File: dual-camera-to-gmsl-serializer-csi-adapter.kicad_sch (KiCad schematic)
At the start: 126 parts, among them J1 Conn_FFC_WE_68715014022, J2 Conn_FFC_WE_68715014022, J3 Conn_FFC_WE_68715014022, J4 JST_SH_1x4_SM04B-SRSS-TB-LF-SN, J5 JST_SH_1x4_SM04B-SRSS-TB-LF-SN, U1 TPS2117DRLR, U2 TPS2117DRLR, U3 AP62301_TSOT

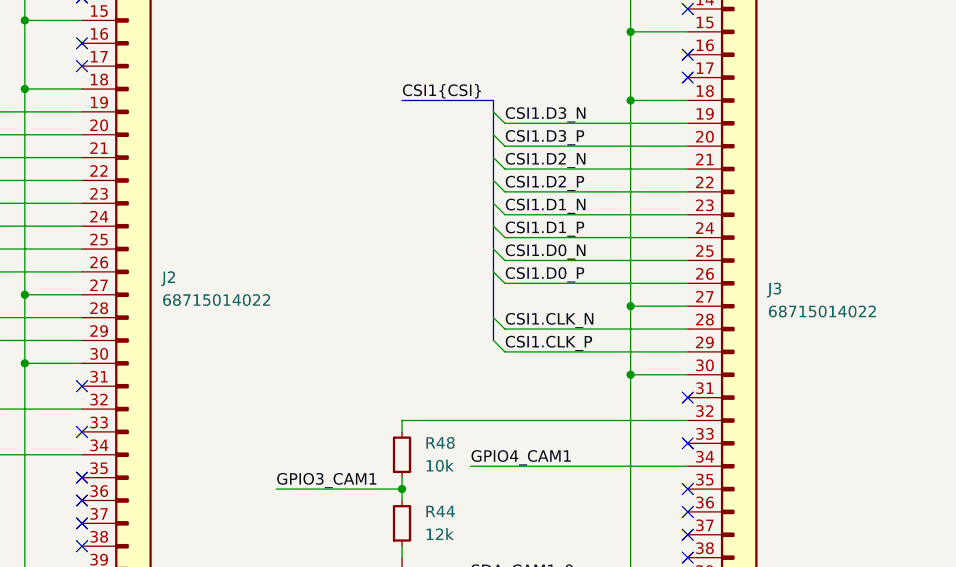
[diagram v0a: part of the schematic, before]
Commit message: [#70359] Schematic: Swap J2 with J3
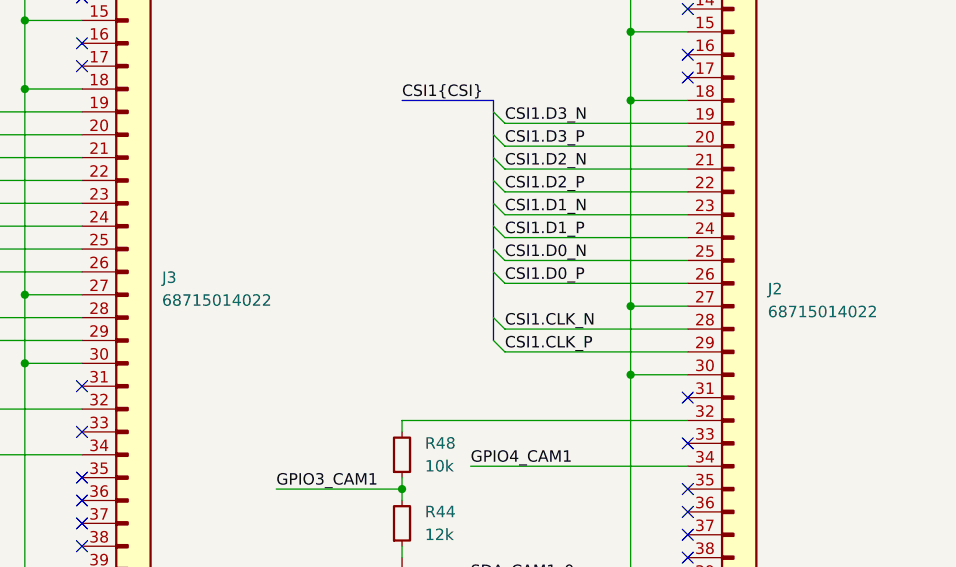
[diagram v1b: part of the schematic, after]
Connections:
- net 3V3_0: now also J3.47, J3.48; no longer J2.47, J2.48
- net 3V3_1: now also J2.47, J2.48; no longer J3.47, J3.48
- net 5V_0: now also J3.49, J3.50; no longer J2.49, J2.50
- net 5V_1: now also J2.49, J2.50; no longer J3.49, J3.50
- net CSI0.CLK_N: now also J3.28; no longer J2.28
- net CSI0.CLK_P: now also J3.29; no longer J2.29
- net CSI0.D0_N: now also J3.25; no longer J2.25
- net CSI0.D0_P: now also J3.26; no longer J2.26
- net CSI0.D1_N: now also J3.23; no longer J2.23
- net CSI0.D1_P: now also J3.24; no longer J2.24
- net CSI0.D2_N: now also J3.21; no longer J2.21
- net CSI0.D2_P: now also J3.22; no longer J2.22
- net CSI0.D3_N: now also J3.19; no longer J2.19
- net CSI0.D3_P: now also J3.20; no longer J2.20
- net CSI1.CLK_N: now also J2.28; no longer J3.28
- net CSI1.CLK_P: now also J2.29; no longer J3.29
- net CSI1.D0_N: now also J2.25; no longer J3.25
- net CSI1.D0_P: now also J2.26; no longer J3.26
- net CSI1.D1_N: now also J2.23; no longer J3.23
- net CSI1.D1_P: now also J2.24; no longer J3.24
- net CSI1.D2_N: now also J2.21; no longer J3.21
- net CSI1.D2_P: now also J2.22; no longer J3.22
- net CSI1.D3_N: now also J2.19; no longer J3.19
- net CSI1.D3_P: now also J2.20; no longer J3.20
- net GPIO2_CAM0: now also J3.34; no longer J2.34
- net GPIO4_CAM1: now also J2.34; no longer J3.34
- net SCL_CAM0_0: now also J3.40; no longer J2.40
- net SCL_CAM0_1: now also J3.42; no longer J2.42
- net SCL_CAM1_0: now also J2.40; no longer J3.40
- net SCL_CAM1_1: now also J2.42; no longer J3.42
- net SDA_CAM0_0: now also J3.39; no longer J2.39
- net SDA_CAM0_1: now also J3.41; no longer J2.41
- net SDA_CAM1_0: now also J2.39; no longer J3.39
- net SDA_CAM1_1: now also J2.41; no longer J3.41
- net at J3.32: now also R47.2; no longer R48.2
- net at J2.32: now also R48.2; no longer R47.2
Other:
- moved on the sheet: J2, J3
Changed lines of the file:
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@@
 	(symbol
 		(lib_id "antmicroFCCConnectors:Conn_FFC_WE_68715014022")
-		(at 372.11 40.64 0)
+		(at 304.8 39.37 0)
 		(unit 1)
 		(exclude_from_sim no)
@@
 		(fields_autoplaced yes)
 		(property "Reference" "J3"
-			(at 381 104.775 0)
+			(at 313.69 103.505 0)
 			(effects
 				(font
@@
 		)
 		(property "Value" "Conn_FFC_WE_68715014022"
-			(at 391.16 48.26 0)
+			(at 323.85 46.99 0)
 			(effects
 				(font
@@
 		)
 		(property "Footprint" "antmicro-footprints:Conn_FFC_WE_68715014x22"
-			(at 391.16 50.8 0)
+			(at 323.85 49.53 0)
 			(effects
 				(font
@@
 		)
 		(property "Datasheet" "https://www.we-online.com/components/products/datasheet/68715014022.pdf"
-			(at 391.16 53.34 0)
+			(at 323.85 52.07 0)
 			(effects
 				(font
@@
 		)
 		(property "Description" "FFC connector"
-			(at 372.11 40.64 0)
+			(at 304.8 39.37 0)
 			(effects
 				(font
@@
 		)
 		(property "MPN" "68715014022"
-			(at 381 107.315 0)
+			(at 313.69 106.045 0)
 			(effects
 				(font
@@
 		)
 		(property "Manufacturer" "Würth Elektronik"
-			(at 391.16 58.42 0)
+			(at 323.85 57.15 0)
 			(effects
 				(font
@@
 		)
 		(property "Author" "Antmicro"
-			(at 391.16 60.96 0)
+			(at 323.85 59.69 0)
 			(effects
 				(font
@@
 		)
 		(property "License" "Apache-2.0"
-			(at 391.16 63.5 0)
+			(at 323.85 62.23 0)
 			(effects
 				(font
@@
 	(symbol
 		(lib_id "antmicroFCCConnectors:Conn_FFC_WE_68715014022")
-		(at 304.8 39.37 0)
+		(at 372.11 40.64 0)
 		(unit 1)
 		(exclude_from_sim no)
@@
 		(fields_autoplaced yes)
 		(property "Reference" "J2"
-			(at 313.69 103.505 0)
+			(at 381 104.775 0)
 			(effects
 				(font
@@
 		)
 		(property "Value" "Conn_FFC_WE_68715014022"
-			(at 323.85 46.99 0)
+			(at 391.16 48.26 0)
 			(effects
 				(font
@@
 		)
 		(property "Footprint" "antmicro-footprints:Conn_FFC_WE_68715014x22"
-			(at 323.85 49.53 0)
+			(at 391.16 50.8 0)
 			(effects
 				(font
@@
 		)
 		(property "Datasheet" "https://www.we-online.com/components/products/datasheet/68715014022.pdf"
-			(at 323.85 52.07 0)
+			(at 391.16 53.34 0)
 			(effects
 				(font
@@
 		)
 		(property "Description" "FFC connector"
-			(at 304.8 39.37 0)
+			(at 372.11 40.64 0)
 			(effects
 				(font
@@
 		)
 		(property "MPN" "68715014022"
-			(at 313.69 106.045 0)
+			(at 381 107.315 0)
 			(effects
 				(font
@@
 		)
 		(property "Manufacturer" "Würth Elektronik"
-			(at 323.85 57.15 0)
+			(at 391.16 58.42 0)
 			(effects
 				(font
@@
 		)
 		(property "Author" "Antmicro"
-			(at 323.85 59.69 0)
+			(at 391.16 60.96 0)
 			(effects
 				(font
@@
 		)
 		(property "License" "Apache-2.0"
-			(at 323.85 62.23 0)
+			(at 391.16 63.5 0)
 			(effects
 				(font

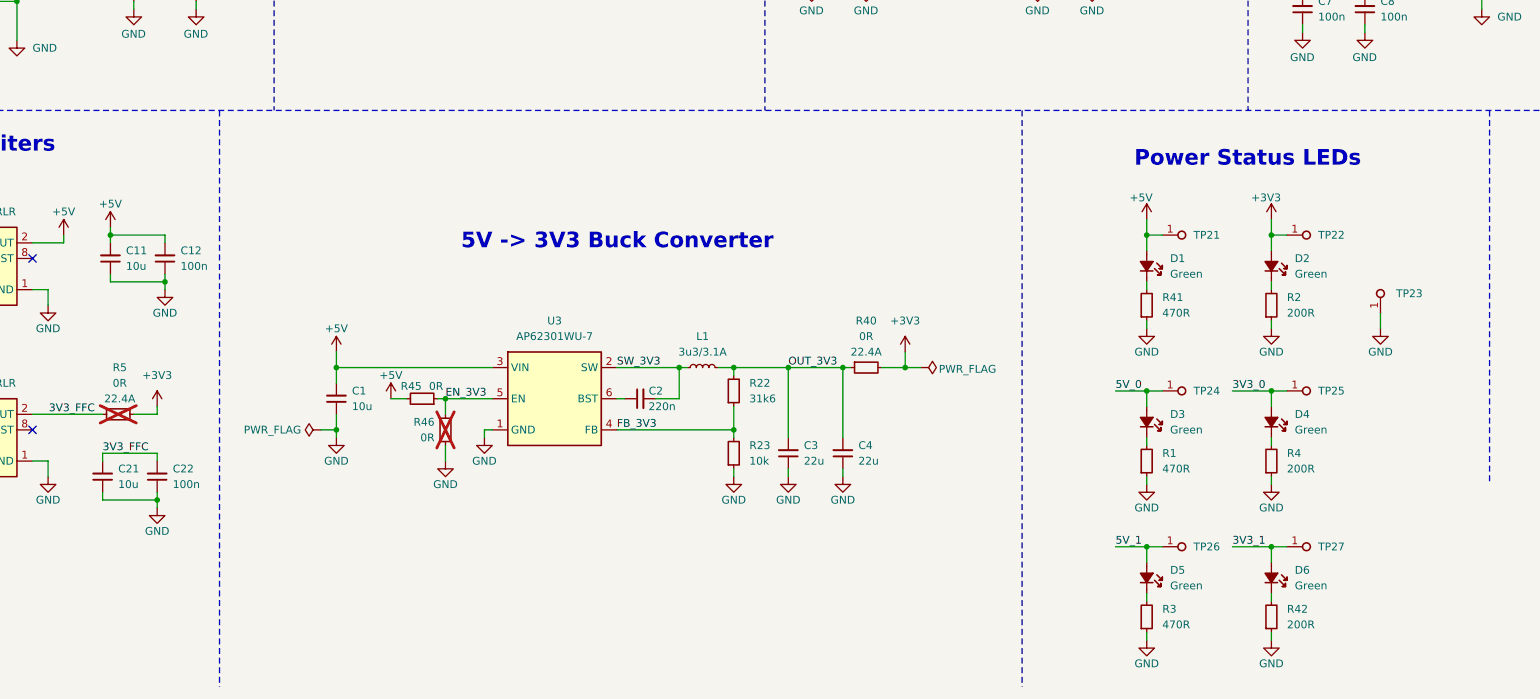
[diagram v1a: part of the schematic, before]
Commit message: [#70359] PCB: Position TPs and logos
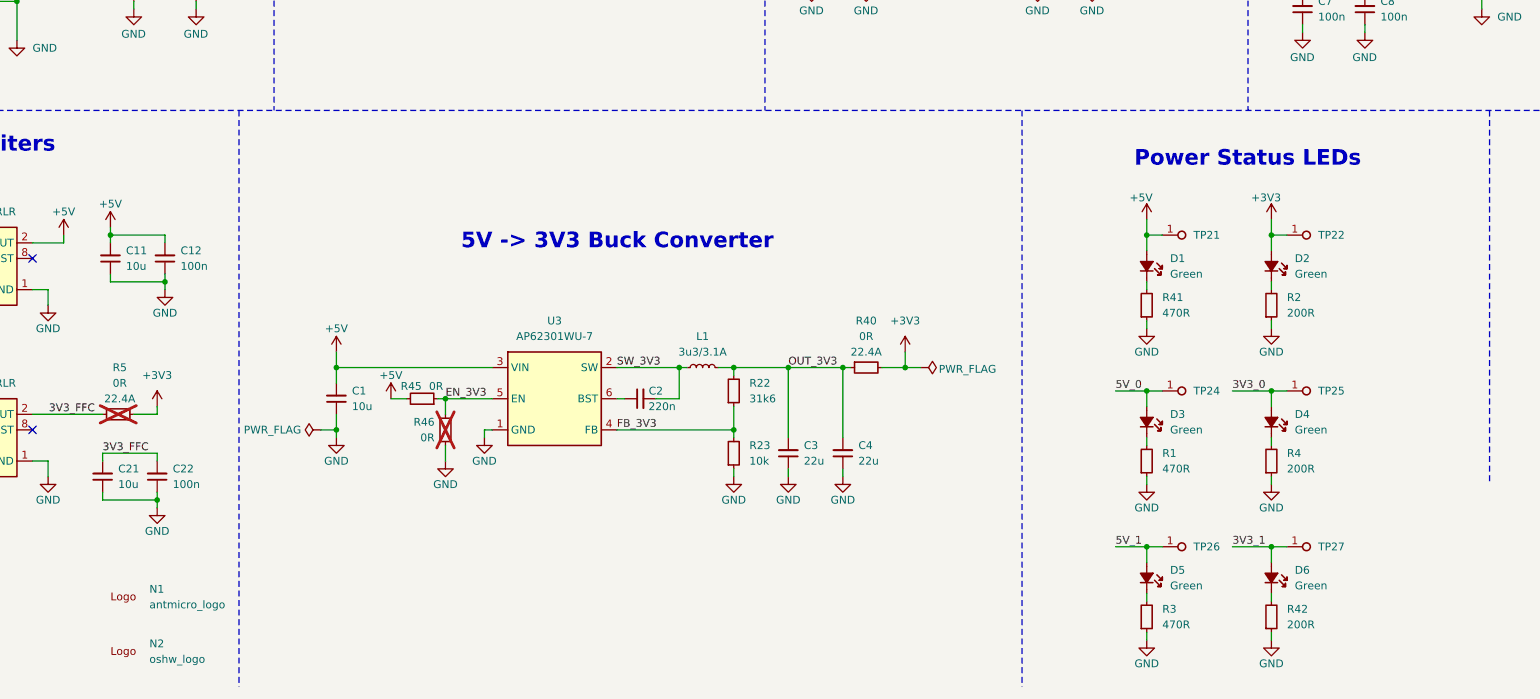
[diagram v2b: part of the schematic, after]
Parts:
- removed TP23: TP_1.5mm_SMD, antmicro-footprints:TP_SMD_1.5mm, symbol antmicroTestPoints:TP_1.5mm_SMD
- added N1: antmicro_logo, antmicro-footprints:antmicro-logo_scaled_12mm, symbol antmicroMechanicalParts:antmicro_logo
- added N2: oshw_logo, antmicro-footprints:oshw-logo, symbol antmicroMechanicalParts:oshw_logo
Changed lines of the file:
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@@
 	(polyline
 		(pts
-			(xy 92.71 191.77) (xy 92.71 285.75)
+			(xy 95.885 191.77) (xy 95.885 285.75)
 		)
 		(stroke
@@
 	(wire
 		(pts
-			(xy 281.94 227.33) (xy 281.94 224.79)
-		)
-		(stroke
-			(width 0)
-			(type default)
-		)
-	)
-	(wire
-		(pts
 			(xy 264.16 245.11) (xy 264.16 246.38)
 		)
@@
 	)
 	(symbol
+		(lib_id "antmicroMechanicalParts:oshw_logo")
+		(at 74.93 280.67 0)
+		(unit 1)
+		(exclude_from_sim no)
+		(in_bom no)
+		(on_board yes)
+		(dnp no)
+		(fields_autoplaced yes)
+		(property "Reference" "N2"
+			(at 81.28 278.6862 0)
+			(effects
+				(font
+					(size 1.27 1.27)
+					(thickness 0.15)
+				)
+				(justify left)
+			)
+		)
+		(property "Value" "oshw_logo"
+			(at 81.28 281.2262 0)
+			(effects
+				(font
+					(size 1.27 1.27)
+					(thickness 0.15)
+				)
+				(justify left)
+			)
+		)
+		(property "Footprint" "antmicro-footprints:oshw-logo"
+			(at 90.17 290.83 0)
+			(effects
+				(font
+					(size 1.27 1.27)
+					(thickness 0.15)
+				)
+				(justify left bottom)
+				(hide yes)
+			)
+		)
+		(property "Datasheet" ""
+			(at 90.17 293.37 0)
+			(effects
+				(font
+					(size 1.27 1.27)
+					(thickness 0.15)
+				)
+				(justify left bottom)
+				(hide yes)
+			)
+		)
+		(property "Description" "Mechanical part"
+			(at 74.93 280.67 0)
+			(effects
+				(font
+					(size 1.27 1.27)
+				)
+				(hide yes)
+			)
+		)
+		(property "Author" "Antmicro"
+			(at 90.17 295.91 0)
+			(effects
+				(font
+					(size 1.27 1.27)
+					(thickness 0.15)
+				)
+				(justify left bottom)
+				(hide yes)
+			)
+		)
+		(property "License" "Apache-2.0"
+			(at 90.17 298.45 0)
+			(effects
+				(font
+					(size 1.27 1.27)
+					(thickness 0.15)
+				)
+				(justify left bottom)
+				(hide yes)
+			)
+		)
+		(property "MPN" ""
+			(at 74.93 280.67 0)
+			(effects
+				(font
+					(size 1.27 1.27)
+				)
+			)
+		)
+		(property "Manufacturer" ""
+			(at 90.17 300.99 0)
+			(effects
+				(font
+					(size 1.27 1.27)
+					(thickness 0.15)
+				)
+				(justify left bottom)
+				(hide yes)
+			)
+		)
+		(instances
+			(project ""
+				(path "/cf1ce08b-3792-4258-a49b-b5b867cae6f7"
+					(reference "N2")
+					(unit 1)
+				)
+			)
+		)
+	)
+	(symbol
 		(lib_id "antmicroResistors0402:R_200R_0402")
 		(at 264.16 251.46 90)
@@
 	)
 	(symbol
+		(lib_id "antmicroMechanicalParts:antmicro_logo")
+		(at 74.93 271.78 0)
+		(unit 1)
+		(exclude_from_sim no)
+		(in_bom no)
+		(on_board yes)
+		(dnp no)
+		(fields_autoplaced yes)
+		(property "Reference" "N1"
+			(at 81.28 269.7962 0)
+			(effects
+				(font
+					(size 1.27 1.27)
+					(thickness 0.15)
+				)
+				(justify left)
+			)
+		)
+		(property "Value" "antmicro_logo"
+			(at 81.28 272.3362 0)
+			(effects
+				(font
+					(size 1.27 1.27)
+					(thickness 0.15)
+				)
+				(justify left)
+			)
+		)
+		(property "Footprint" "antmicro-footprints:antmicro-logo_scaled_12mm"
+			(at 90.17 281.94 0)
+			(effects
+				(font
+					(size 1.27 1.27)
+					(thickness 0.15)
+				)
+				(justify left bottom)
+				(hide yes)
+			)
+		)
+		(property "Datasheet" ""
+			(at 90.17 284.48 0)
+			(effects
+				(font
+					(size 1.27 1.27)
+					(thickness 0.15)
+				)
+				(justify left bottom)
+				(hide yes)
+			)
+		)
+		(property "Description" "Mechanical part"
+			(at 74.93 271.78 0)
+			(effects
+				(font
+					(size 1.27 1.27)
+				)
+				(hide yes)
+			)
+		)
+		(property "MPN" ""
+			(at 74.93 271.78 0)
+			(effects
+				(font
+					(size 1.27 1.27)
+				)
+			)
+		)
+		(property "Manufacturer" ""
+			(at 90.17 292.1 0)
+			(effects
+				(font
+					(size 1.27 1.27)
+					(thickness 0.15)
+				)
+				(justify left bottom)
+				(hide yes)
+			)
+		)
+		(property "Author" "Antmicro"
+			(at 90.17 287.02 0)
+			(effects
+				(font
+					(size 1.27 1.27)
+					(thickness 0.15)
+				)
+				(justify left bottom)
+				(hide yes)
+			)
+		)
+		(property "License" "Apache-2.0"
+			(at 90.17 289.56 0)
+			(effects
+				(font
+					(size 1.27 1.27)
+					(thickness 0.15)
+				)
+				(justify left bottom)
+				(hide yes)
+			)
+		)
+		(instances
+			(project ""
+				(path "/cf1ce08b-3792-4258-a49b-b5b867cae6f7"
+					(reference "N1")
+					(unit 1)
+				)
+			)
+		)
+	)
+	(symbol
 		(lib_id "antmicropower:GND")
 		(at 337.82 179.07 0)
@@
 	)
 	(symbol
-		(lib_id "antmicroTestPoints:TP_1.5mm_SMD")
-		(at 281.94 224.79 90)
-		(unit 1)
-		(exclude_from_sim no)
-		(in_bom no)
-		(on_board yes)
-		(dnp no)
-		(fields_autoplaced yes)
-		(property "Reference" "TP23"
-			(at 284.48 221.615 90)
-			(effects
-				(font
-					(size 1.27 1.27)
-					(thickness 0.15)
-				)
-				(justify right)
-			)
-		)
-		(property "Value" "TP_1.5mm_SMD"
-			(at 289.56 209.55 0)
-			(effects
-				(font
-					(size 1.27 1.27)
-					(thickness 0.15)
-				)
-				(justify left bottom)
-				(hide yes)
-			)
-		)
-		(property "Footprint" "antmicro-footprints:TP_SMD_1.5mm"
-			(at 292.1 209.55 0)
-			(effects
-				(font
-					(size 1.27 1.27)
-					(thickness 0.15)
-				)
-				(justify left bottom)
-				(hide yes)
-			)
-		)
-		(property "Datasheet" ""
-			(at 294.64 207.01 0)
-			(effects
-				(font
-					(size 1.27 1.27)
-					(thickness 0.15)
-				)
-				(justify left bottom)
-				(hide yes)
-			)
-		)
-		(property "Description" "test point, SMT"
-			(at 281.94 224.79 0)
-			(effects
-				(font
-					(size 1.27 1.27)
-				)
-				(hide yes)
-			)
-		)
-		(property "MPN" ""
-			(at 281.94 224.79 0)
-			(effects
-				(font
-					(size 1.27 1.27)
-				)
-				(hide yes)
-			)
-		)
-		(property "Manufacturer" ""
-			(at 281.94 224.79 0)
-			(effects
-				(font
-					(size 1.27 1.27)
-				)
-				(hide yes)
-			)
-		)
-		(property "Author" "Antmicro"
-			(at 297.18 209.55 0)
-			(effects
-				(font
-					(size 1.27 1.27)
-					(thickness 0.15)
-				)
-				(justify left bottom)
-				(hide yes)
-			)
-		)
-		(property "License" "Apache-2.0"
-			(at 299.72 209.55 0)
-			(effects
-				(font
-					(size 1.27 1.27)
-					(thickness 0.15)
-				)
-				(justify left bottom)
-				(hide yes)
-			)
-		)
-		(pin "1"
-		)
-		(instances
-			(project "dual-camera-to-gmsl-serializer-csi-adapter"
-				(path "/cf1ce08b-3792-4258-a49b-b5b867cae6f7"
-					(reference "TP23")
-					(unit 1)
-				)
-			)
-		)
-	)
-	(symbol
 		(lib_id "antmicropower:GND")
 		(at 204.47 162.56 0)
@@
 					(unit 1)
 				)
-			)
-		)
-	)
-	(symbol
-		(lib_id "antmicropower:GND")
-		(at 281.94 227.33 0)
-		(unit 1)
-		(exclude_from_sim no)
-		(in_bom yes)
-		(on_board yes)
-		(dnp no)
-		(property "Reference" "#PWR023"
-			(at 290.83 229.87 0)
-			(effects
-				(font
-					(size 1.27 1.27)
-					(thickness 0.15)
-				)
-				(justify left bottom)
-				(hide yes)
-			)
-		)
-		(property "Value" "GND"
-			(at 281.94 231.14 0)
-			(effects
-				(font
-					(size 1.27 1.27)
-					(thickness 0.15)
-				)
-			)
-		)
-		(property "Footprint" ""
-			(at 290.83 234.95 0)
-			(effects
-				(font
-					(size 1.27 1.27)
-					(thickness 0.15)
-				)
-				(justify left bottom)
-				(hide yes)
-			)
-		)
-		(property "Datasheet" ""
-			(at 290.83 240.03 0)
-			(effects
-				(font
-					(size 1.27 1.27)
-					(thickness 0.15)
-				)
-				(justify left bottom)
-				(hide yes)
-			)
-		)
-		(property "Description" ""
-			(at 281.94 227.33 0)
-			(effects
-				(font
-					(size 1.27 1.27)
-				)
-				(hide yes)
-			)
-		)
-		(property "Author" "Antmicro"
-			(at 290.83 234.95 0)
-			(effects
-				(font
-					(size 1.27 1.27)
-					(thickness 0.15)
-				)
-				(justify left bottom)
-				(hide yes)
-			)
-		)
-		(property "License" "Apache-2.0"
-			(at 290.83 237.49 0)
-			(effects
-				(font
-					(size 1.27 1.27)
-					(thickness 0.15)
-				)
-				(justify left bottom)
-				(hide yes)
-			)
-		)
-		(pin "1"
-		)
-		(instances
-			(project "dual-camera-to-gmsl-serializer-csi-adapter"
-				(path "/cf1ce08b-3792-4258-a49b-b5b867cae6f7"
-					(reference "#PWR023")
-					(unit 1)
-				)
